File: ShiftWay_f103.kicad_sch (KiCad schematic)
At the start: 0 parts

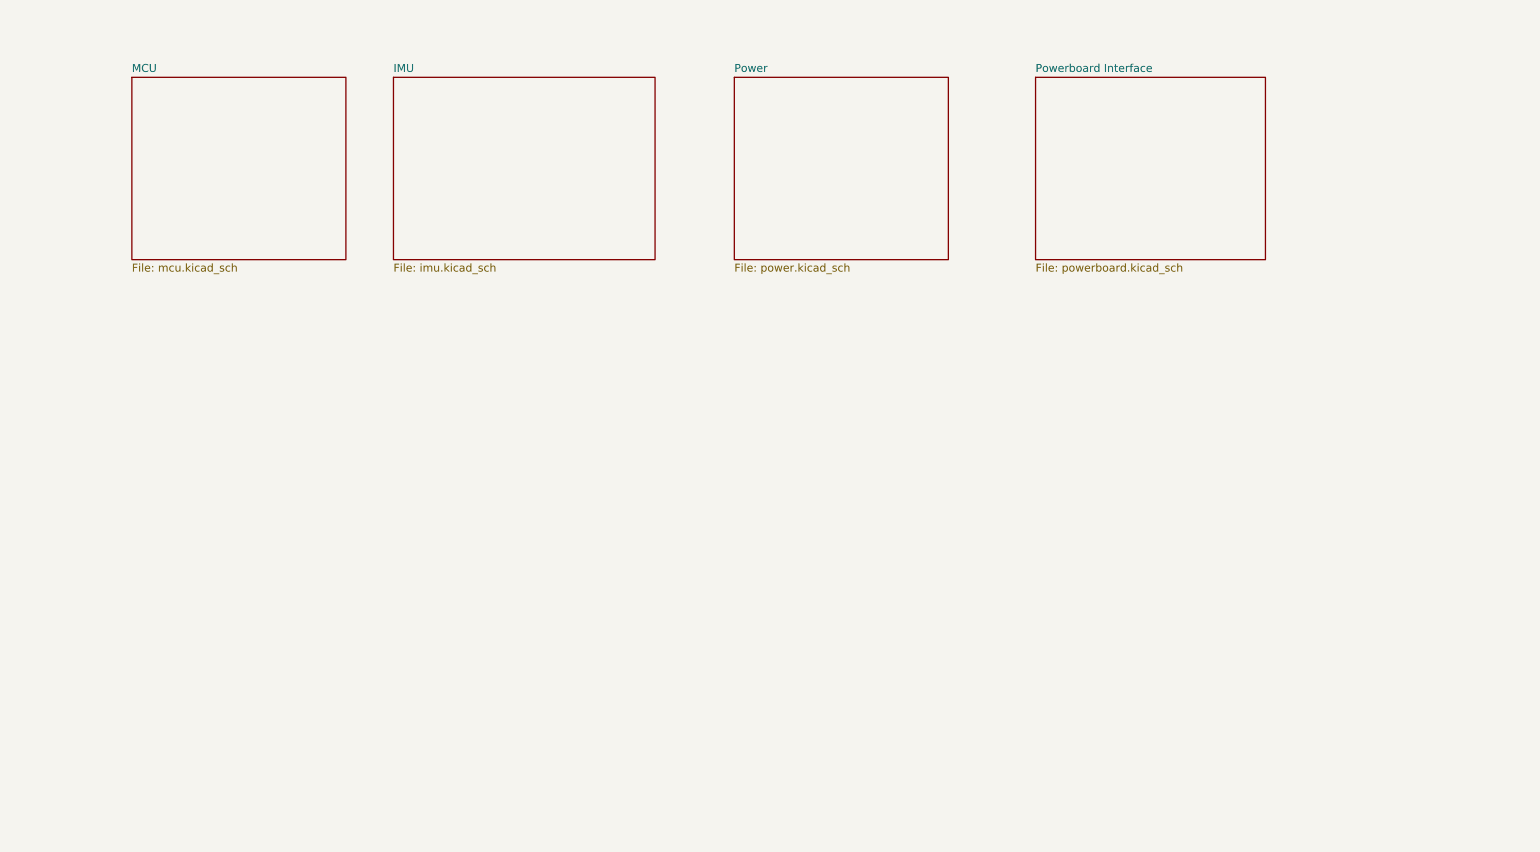
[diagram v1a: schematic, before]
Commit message: Divider, gate, mtr button, testpoints, minors
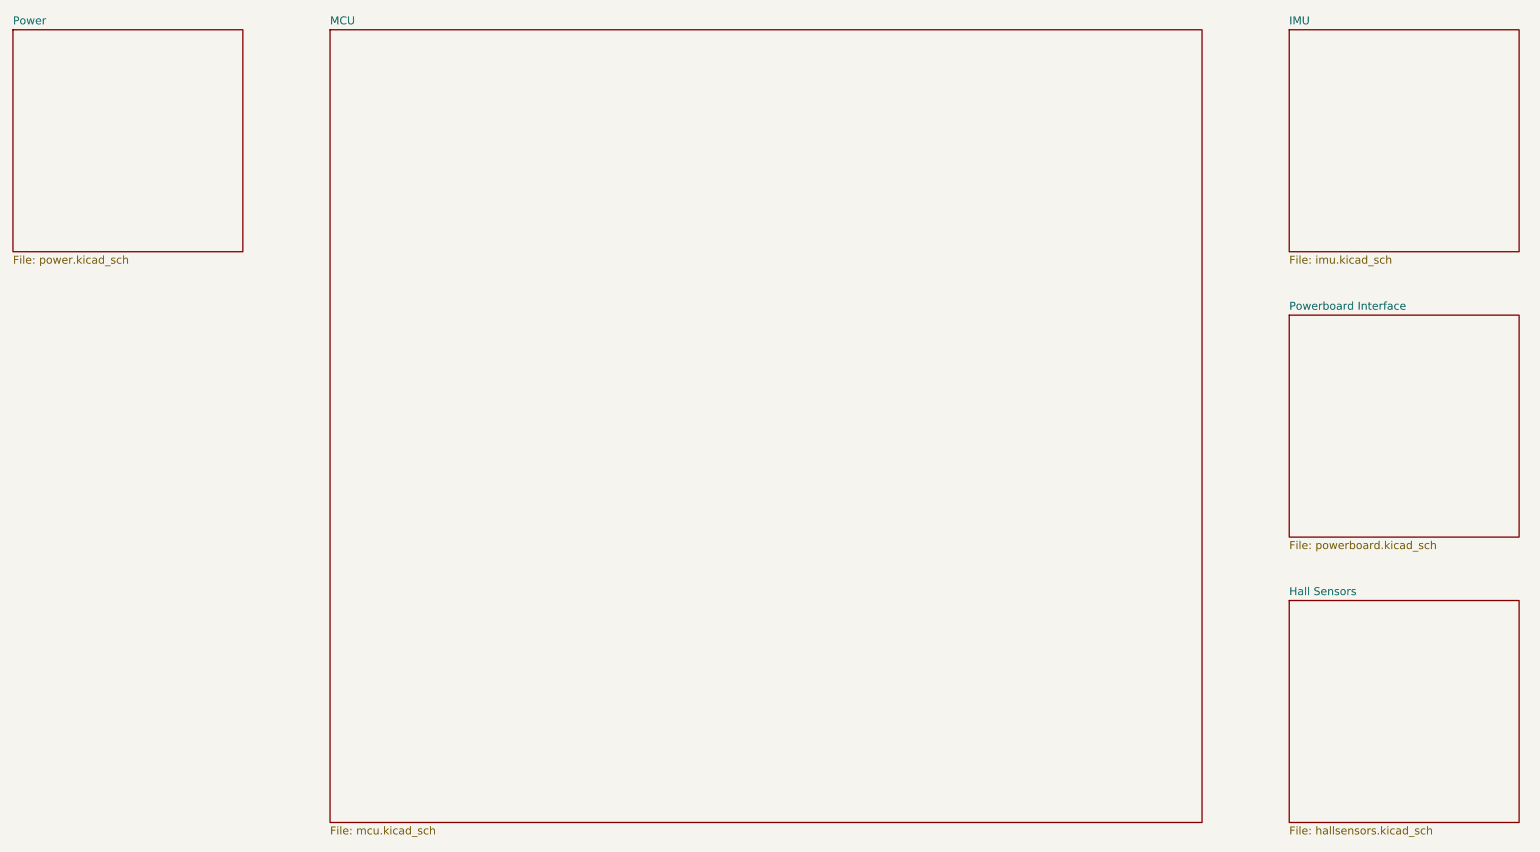
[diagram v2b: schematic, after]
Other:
- added sheet Hall Sensors (hallsensors.kicad_sch)
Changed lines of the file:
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@@
 (kicad_sch (version 20230121) (generator eeschema)
   (paper "A4")
-  (sheet (at 44.45 33.02) (size 34.29 29.21) (fields_autoplaced)
+  (sheet (at 76.2 25.4) (size 139.7 127) (fields_autoplaced)
     (stroke (width 0.1524) (type solid))
     (fill (color 0 0 0 0.0000))
-    (property "Sheetname" "MCU" (at 44.45 32.3084 0)
+    (property "Sheetname" "MCU" (at 76.2 24.6884 0)
       (effects (font (size 1.27 1.27)) (justify left bottom))
     )
-    (property "Sheetfile" "mcu.kicad_sch" (at 44.45 62.8146 0)
+    (property "Sheetfile" "mcu.kicad_sch" (at 76.2 152.9846 0)
       (effects (font (size 1.27 1.27)) (justify left top))
     )
@@
     )
   )
-  (sheet (at 189.23 33.02) (size 36.83 29.21) (fields_autoplaced)
+  (sheet (at 229.87 71.12) (size 36.83 35.56) (fields_autoplaced)
     (stroke (width 0.1524) (type solid))
     (fill (color 0 0 0 0.0000))
-    (property "Sheetname" "Powerboard Interface" (at 189.23 32.3084 0)
+    (property "Sheetname" "Powerboard Interface" (at 229.87 70.4084 0)
       (effects (font (size 1.27 1.27)) (justify left bottom))
     )
-    (property "Sheetfile" "powerboard.kicad_sch" (at 189.23 62.8146 0)
+    (property "Sheetfile" "powerboard.kicad_sch" (at 229.87 107.2646 0)
       (effects (font (size 1.27 1.27)) (justify left top))
     )
@@
     )
   )
-  (sheet (at 140.97 33.02) (size 34.29 29.21) (fields_autoplaced)
+  (sheet (at 25.4 25.4) (size 36.83 35.56) (fields_autoplaced)
     (stroke (width 0.1524) (type solid))
     (fill (color 0 0 0 0.0000))
-    (property "Sheetname" "Power" (at 140.97 32.3084 0)
+    (property "Sheetname" "Power" (at 25.4 24.6884 0)
       (effects (font (size 1.27 1.27)) (justify left bottom))
     )
-    (property "Sheetfile" "power.kicad_sch" (at 140.97 62.8146 0)
+    (property "Sheetfile" "power.kicad_sch" (at 25.4 61.5446 0)
       (effects (font (size 1.27 1.27)) (justify left top))
     )
@@
     )
   )
-  (sheet (at 86.36 33.02) (size 41.91 29.21) (fields_autoplaced)
+  (sheet (at 229.87 25.4) (size 36.83 35.56) (fields_autoplaced)
     (stroke (width 0.1524) (type solid))
     (fill (color 0 0 0 0.0000))
-    (property "Sheetname" "IMU" (at 86.36 32.3084 0)
+    (property "Sheetname" "IMU" (at 229.87 24.6884 0)
       (effects (font (size 1.27 1.27)) (justify left bottom))
     )
-    (property "Sheetfile" "imu.kicad_sch" (at 86.36 62.8146 0)
+    (property "Sheetfile" "imu.kicad_sch" (at 229.87 61.5446 0)
       (effects (font (size 1.27 1.27)) (justify left top))
     )
@@
       )
     )
+  )
+  (sheet (at 229.87 116.84) (size 36.83 35.56) (fields_autoplaced)
+    (stroke (width 0.1524) (type solid))
+    (fill (color 0 0 0 0.0000))
+    (property "Sheetname" "Hall Sensors" (at 229.87 116.1284 0)
+      (effects (font (size 1.27 1.27)) (justify left bottom))
+    )
+    (property "Sheetfile" "hallsensors.kicad_sch" (at 229.87 152.9846 0)
+      (effects (font (size 1.27 1.27)) (justify left top))
+    )
+    (instances
+      (project "ShiftWay_f103"
+        (path "/c57bc97c-1c43-4bb1-9424-fed846030b7b" (page "6"))
+      )
+    )

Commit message: Minors, annotation
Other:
- title: (none) -> RedShift-117.6-LogicBoard-F103
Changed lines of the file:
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@@
 (kicad_sch (version 20230121) (generator eeschema)
   (paper "A4")
+  (title_block
+    (title "RedShift-117.6-LogicBoard-F103")
+    (date "08.12.2023")
+    (rev "0.1")
+  )
   (sheet (at 76.2 25.4) (size 139.7 127) (fields_autoplaced)
     (stroke (width 0.1524) (type solid))

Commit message: Fix mistakes
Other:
- sheet Power renamed Power Inlet
- added sheet Power Stepdowns (stepdowns.kicad_sch)
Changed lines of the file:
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@@
     (instances
       (project "ShiftWay_f103"
-        (path "/c57bc97c-1c43-4bb1-9424-fed846030b7b" (page "2"))
+        (path "/c57bc97c-1c43-4bb1-9424-fed846030b7b" (page "3"))
       )
     )
@@
     )
   )
-  (sheet (at 25.4 25.4) (size 36.83 35.56) (fields_autoplaced)
+  (sheet (at 25.4 48.26) (size 36.83 29.21) (fields_autoplaced)
     (stroke (width 0.1524) (type solid))
     (fill (color 0 0 0 0.0000))
-    (property "Sheetname" "Power" (at 25.4 24.6884 0)
+    (property "Sheetname" "Power Inlet" (at 25.4 47.5484 0)
       (effects (font (size 1.27 1.27)) (justify left bottom))
     )
-    (property "Sheetfile" "power.kicad_sch" (at 25.4 61.5446 0)
+    (property "Sheetfile" "power.kicad_sch" (at 25.4 78.0546 0)
       (effects (font (size 1.27 1.27)) (justify left top))
     )
@@
       (project "ShiftWay_f103"
         (path "/c57bc97c-1c43-4bb1-9424-fed846030b7b" (page "1"))
+      )
+    )
+  )
+  (sheet (at 25.4 90.17) (size 36.83 27.94) (fields_autoplaced)
+    (stroke (width 0.1524) (type solid))
+    (fill (color 0 0 0 0.0000))
+    (property "Sheetname" "Power Stepdowns" (at 25.4 89.4584 0)
+      (effects (font (size 1.27 1.27)) (justify left bottom))
+    )
+    (property "Sheetfile" "stepdowns.kicad_sch" (at 25.4 118.6946 0)
+      (effects (font (size 1.27 1.27)) (justify left top))
+    )
+    (instances
+      (project "ShiftWay_f103"
+        (path "/c57bc97c-1c43-4bb1-9424-fed846030b7b" (page "2"))
       )
     )
@@
   )
   (sheet_instances
-    (path "/" (page "1"))
+    (path "/" (page "3"))
   )
 )

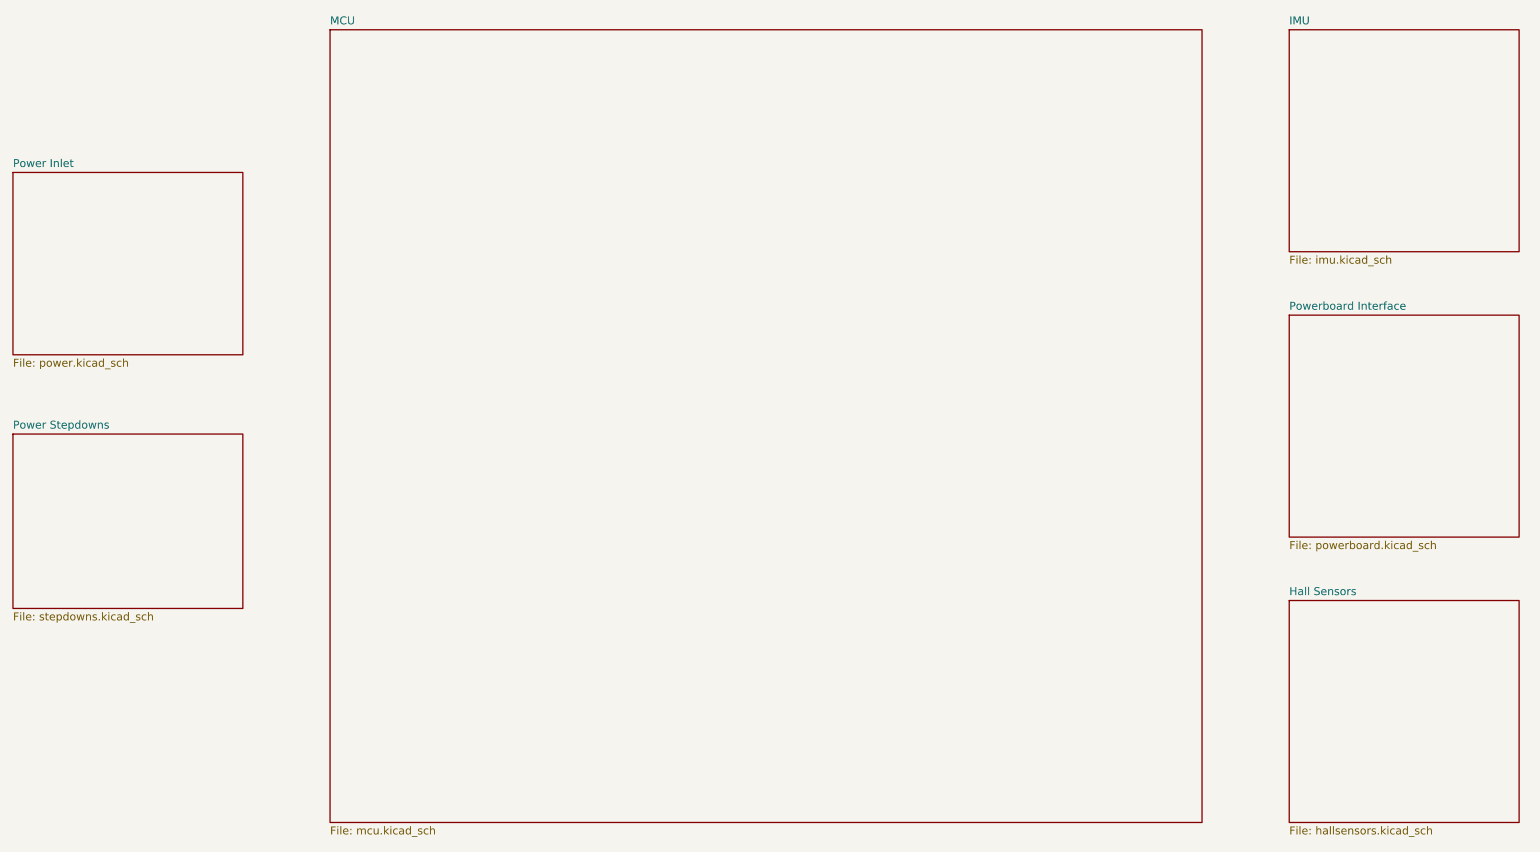
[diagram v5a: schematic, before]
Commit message: Add drivers, stepdown on VIPER115, fixes
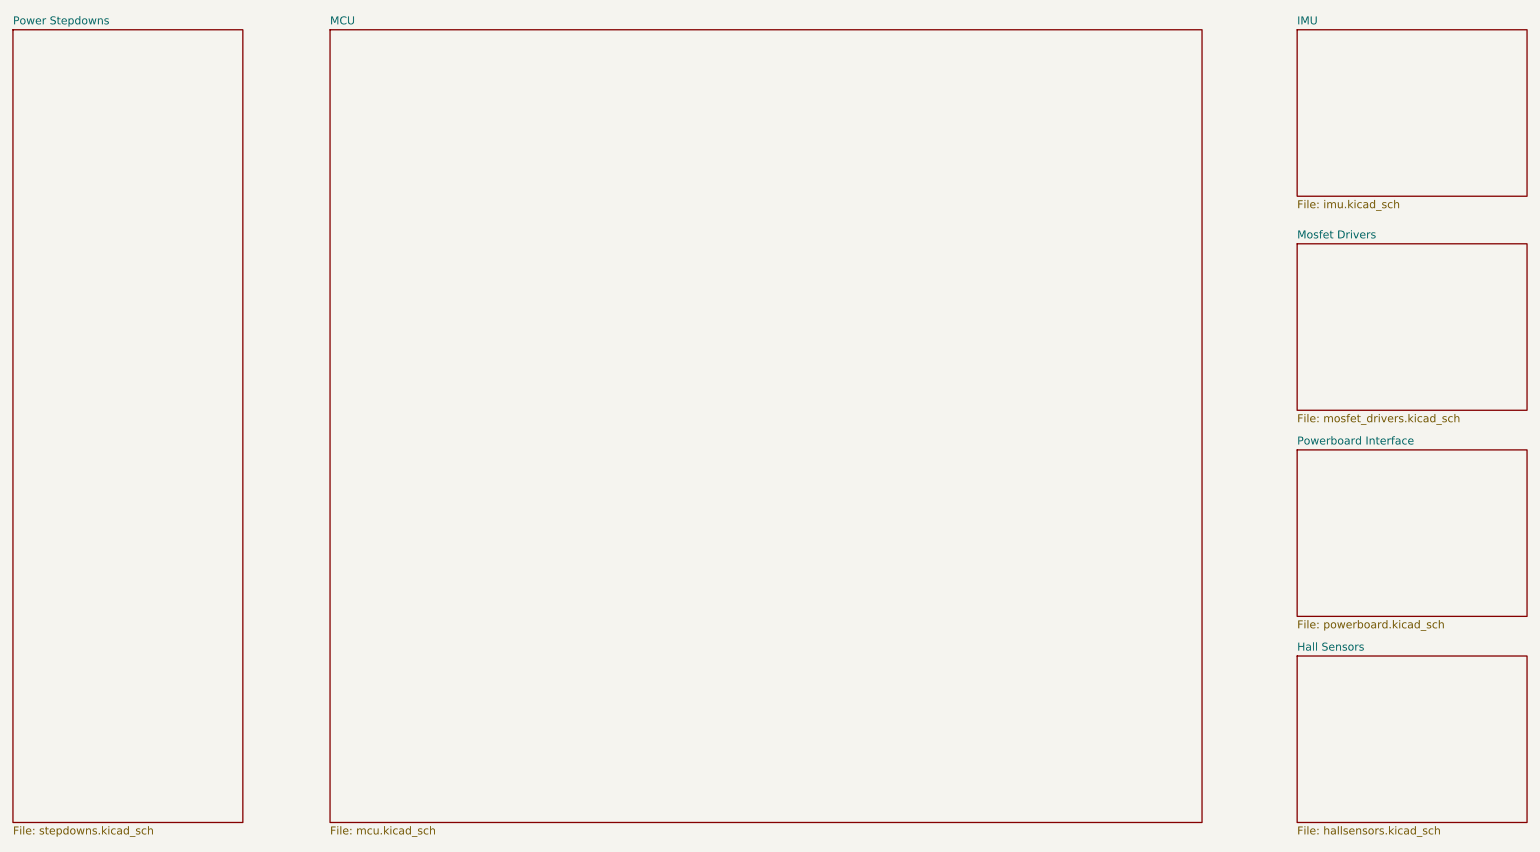
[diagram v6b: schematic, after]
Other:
- removed sheet Power Inlet
- added sheet Mosfet Drivers (mosfet_drivers.kicad_sch)
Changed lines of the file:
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@@
+    (instances
+      (project "ShiftWay_f103"
+        (path "/c57bc97c-1c43-4bb1-9424-fed846030b7b" (page "2"))
+      )
+    )
+  )
+  (sheet (at 231.14 92.71) (size 36.83 26.67) (fields_autoplaced)
+    (stroke (width 0.1524) (type solid))
+    (fill (color 0 0 0 0.0000))
+    (property "Sheetname" "Powerboard Interface" (at 231.14 91.9984 0)
+      (effects (font (size 1.27 1.27)) (justify left bottom))
+    )
+    (property "Sheetfile" "powerboard.kicad_sch" (at 231.14 119.9646 0)
+      (effects (font (size 1.27 1.27)) (justify left top))
+    )
+    (instances
+      (project "ShiftWay_f103"
+        (path "/c57bc97c-1c43-4bb1-9424-fed846030b7b" (page "6"))
+      )
+    )
+  )
+  (sheet (at 25.4 25.4) (size 36.83 127) (fields_autoplaced)
+    (stroke (width 0.1524) (type solid))
+    (fill (color 0 0 0 0.0000))
+    (property "Sheetname" "Power Stepdowns" (at 25.4 24.6884 0)
+      (effects (font (size 1.27 1.27)) (justify left bottom))
+    )
+    (property "Sheetfile" "stepdowns.kicad_sch" (at 25.4 152.9846 0)
+      (effects (font (size 1.27 1.27)) (justify left top))
+    )
+    (instances
+      (project "ShiftWay_f103"
+        (path "/c57bc97c-1c43-4bb1-9424-fed846030b7b" (page "1"))
+      )
+    )
+  )
+  (sheet (at 231.14 25.4) (size 36.83 26.67) (fields_autoplaced)
+    (stroke (width 0.1524) (type solid))
+    (fill (color 0 0 0 0.0000))
+    (property "Sheetname" "IMU" (at 231.14 24.6884 0)
+      (effects (font (size 1.27 1.27)) (justify left bottom))
+    )
+    (property "Sheetfile" "imu.kicad_sch" (at 231.14 52.6546 0)
+      (effects (font (size 1.27 1.27)) (justify left top))
+    )
     (instances
       (project "ShiftWay_f103"
@@
     )
   )
-  (sheet (at 229.87 71.12) (size 36.83 35.56) (fields_autoplaced)
+  (sheet (at 231.14 125.73) (size 36.83 26.67) (fields_autoplaced)
     (stroke (width 0.1524) (type solid))
     (fill (color 0 0 0 0.0000))
-    (property "Sheetname" "Powerboard Interface" (at 229.87 70.4084 0)
+    (property "Sheetname" "Hall Sensors" (at 231.14 125.0184 0)
       (effects (font (size 1.27 1.27)) (justify left bottom))
     )
-    (property "Sheetfile" "powerboard.kicad_sch" (at 229.87 107.2646 0)
+    (property "Sheetfile" "hallsensors.kicad_sch" (at 231.14 152.9846 0)
       (effects (font (size 1.27 1.27)) (justify left top))
     )
@@
     )
   )
-  (sheet (at 25.4 48.26) (size 36.83 29.21) (fields_autoplaced)
+  (sheet (at 231.14 59.69) (size 36.83 26.67) (fields_autoplaced)
     (stroke (width 0.1524) (type solid))
     (fill (color 0 0 0 0.0000))
-    (property "Sheetname" "Power Inlet" (at 25.4 47.5484 0)
+    (property "Sheetname" "Mosfet Drivers" (at 231.14 58.9784 0)
       (effects (font (size 1.27 1.27)) (justify left bottom))
     )
-    (property "Sheetfile" "power.kicad_sch" (at 25.4 78.0546 0)
+    (property "Sheetfile" "mosfet_drivers.kicad_sch" (at 231.14 86.9446 0)
       (effects (font (size 1.27 1.27)) (justify left top))
     )
-    (instances
-      (project "ShiftWay_f103"
-        (path "/c57bc97c-1c43-4bb1-9424-fed846030b7b" (page "1"))
-      )
-    )
-  )
-  (sheet (at 25.4 90.17) (size 36.83 27.94) (fields_autoplaced)
-    (stroke (width 0.1524) (type solid))
-    (fill (color 0 0 0 0.0000))
-    (property "Sheetname" "Power Stepdowns" (at 25.4 89.4584 0)
-      (effects (font (size 1.27 1.27)) (justify left bottom))
-    )
-    (property "Sheetfile" "stepdowns.kicad_sch" (at 25.4 118.6946 0)
-      (effects (font (size 1.27 1.27)) (justify left top))
-    )
-    (instances
-      (project "ShiftWay_f103"
-        (path "/c57bc97c-1c43-4bb1-9424-fed846030b7b" (page "2"))
-      )
-    )
-  )
-  (sheet (at 229.87 25.4) (size 36.83 35.56) (fields_autoplaced)
-    (stroke (width 0.1524) (type solid))
-    (fill (color 0 0 0 0.0000))
-    (property "Sheetname" "IMU" (at 229.87 24.6884 0)
-      (effects (font (size 1.27 1.27)) (justify left bottom))
-    )
-    (property "Sheetfile" "imu.kicad_sch" (at 229.87 61.5446 0)
-      (effects (font (size 1.27 1.27)) (justify left top))
+    (property "Field2" "" (at 231.14 59.69 0)
+      (effects (font (size 1.27 1.27)) hide)
     )
     (instances
@@
     )
   )
-  (sheet (at 229.87 116.84) (size 36.83 35.56) (fields_autoplaced)
-    (stroke (width 0.1524) (type solid))
-    (fill (color 0 0 0 0.0000))
-    (property "Sheetname" "Hall Sensors" (at 229.87 116.1284 0)
-      (effects (font (size 1.27 1.27)) (justify left bottom))
-    )
-    (property "Sheetfile" "hallsensors.kicad_sch" (at 229.87 152.9846 0)
-      (effects (font (size 1.27 1.27)) (justify left top))
-    )
-    (instances
-      (project "ShiftWay_f103"
-        (path "/c57bc97c-1c43-4bb1-9424-fed846030b7b" (page "6"))
-      )
-    )
-  )
   (sheet_instances
-    (path "/" (page "3"))
+    (path "/" (page "0"))
   )
 )
